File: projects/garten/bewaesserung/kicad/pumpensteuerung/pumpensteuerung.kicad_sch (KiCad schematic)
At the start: 9 parts, among them J101 Screw_Terminal_01x02, U101 LM2575-5.0BT

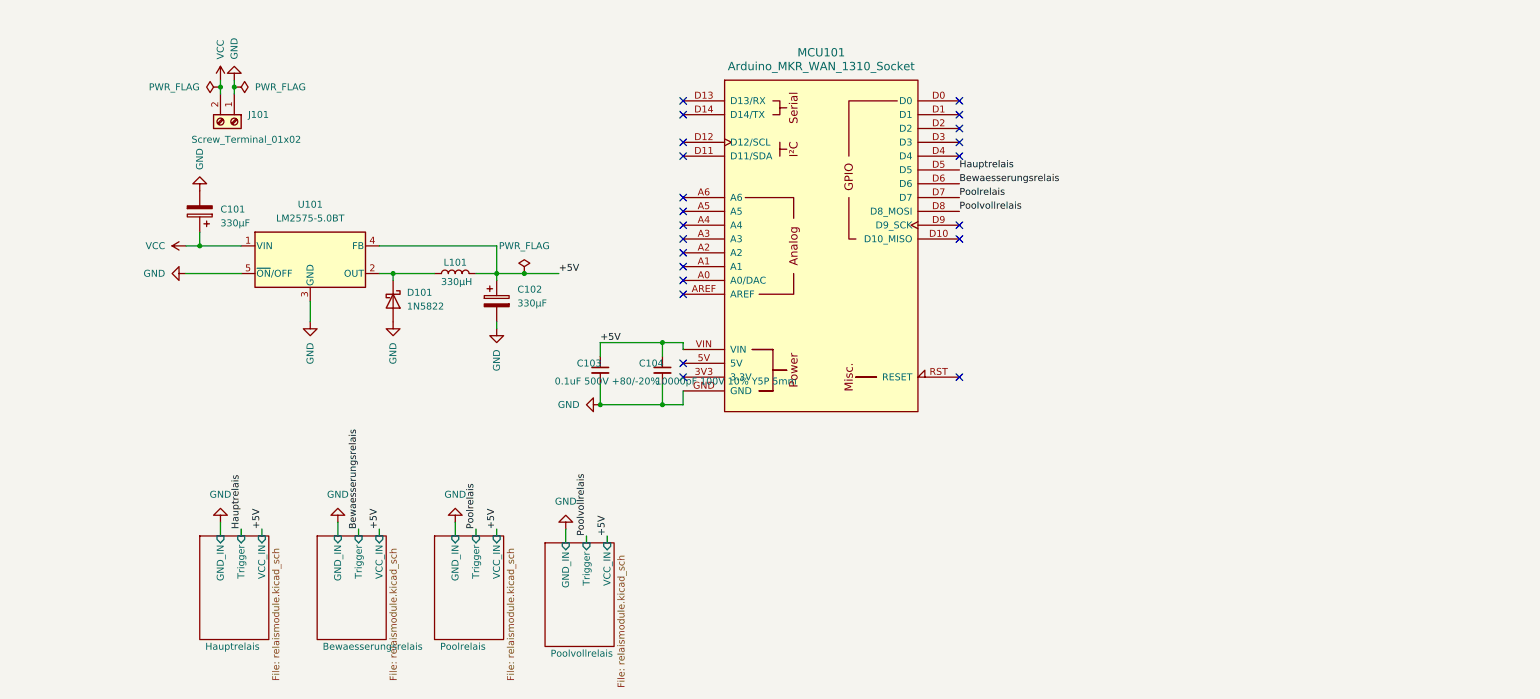
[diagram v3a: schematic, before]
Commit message: [garten/bewaesserung(pcb)] remove capacitor and more space at the top
bloed wenn man nicht misst und gehaeuse und pcb unabhaenig desgin und so
dann erst wenn es fertig ist feststellt da passt etwas nicht. wobei der
arduino ja auch im 3d model des pcb fehlt :(.
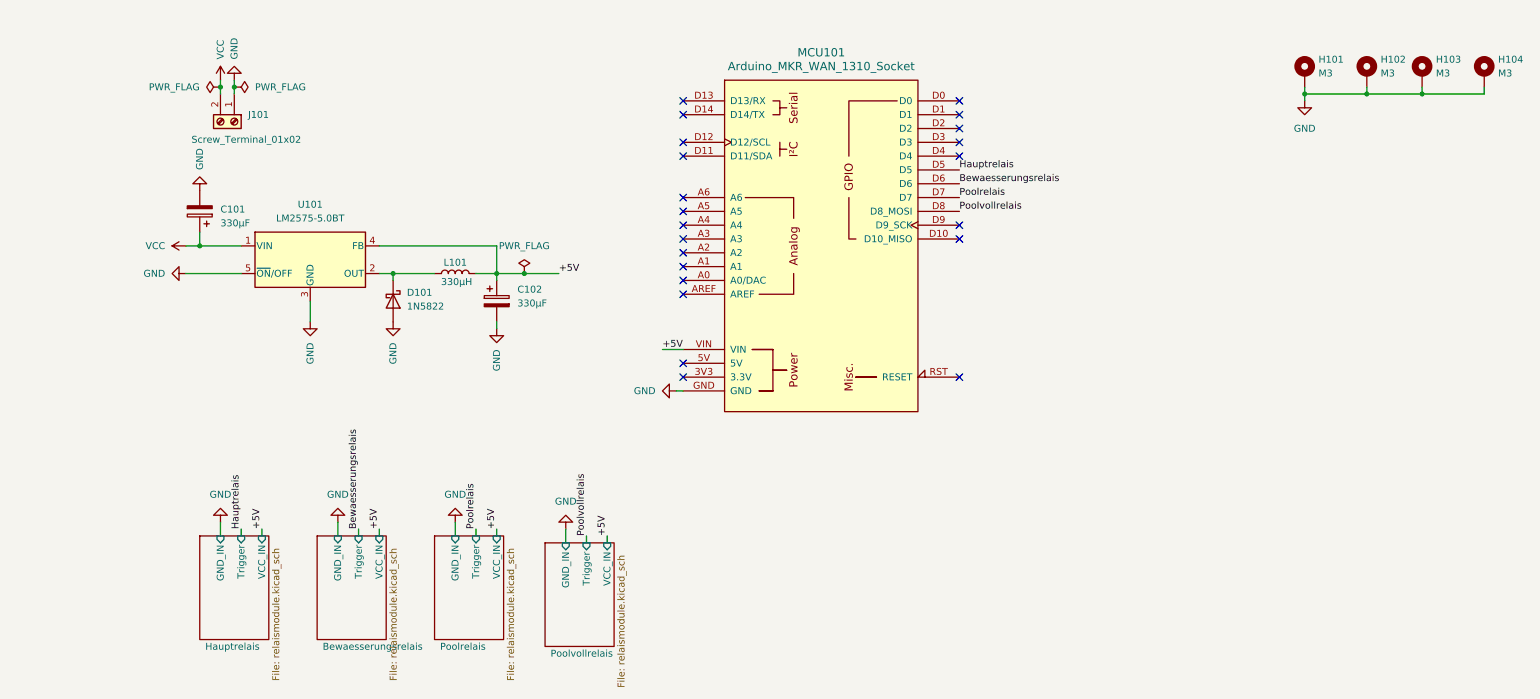
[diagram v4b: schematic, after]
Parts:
- removed C103: 0.1uF 500V +80/-20%, Capacitor_THT:C_Disc_D5.0mm_W2.5mm_P5.00mm, symbol Device:C_Small
- removed C104: 10000pF 100V 10% Y5P 5mm, Capacitor_THT:C_Disc_D5.0mm_W2.5mm_P5.00mm, symbol Device:C_Small
- added H101, H103: M3, MountingHole:MountingHole_3.2mm_M3_Pad_Via, symbol Mechanical:MountingHole_Pad
- added H102, H104: M3, symbol Mechanical:MountingHole_Pad
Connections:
- net GND: now also H101.1, H102.1, H103.1, H104.1
